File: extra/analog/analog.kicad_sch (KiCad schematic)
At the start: 0 parts

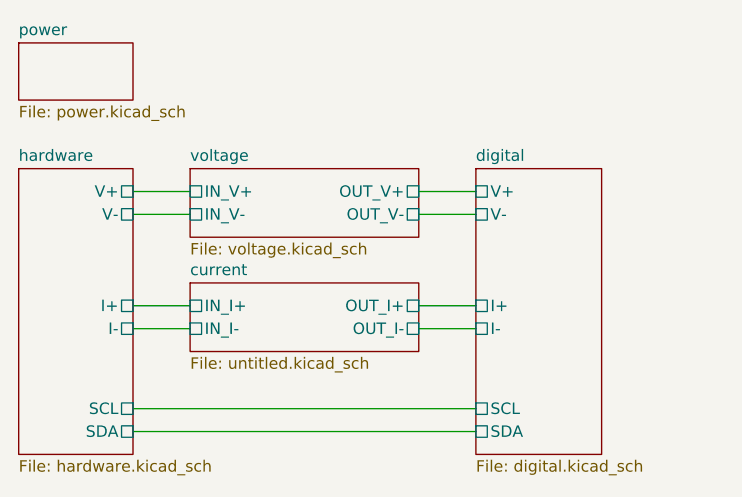
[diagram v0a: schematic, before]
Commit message: Added component values
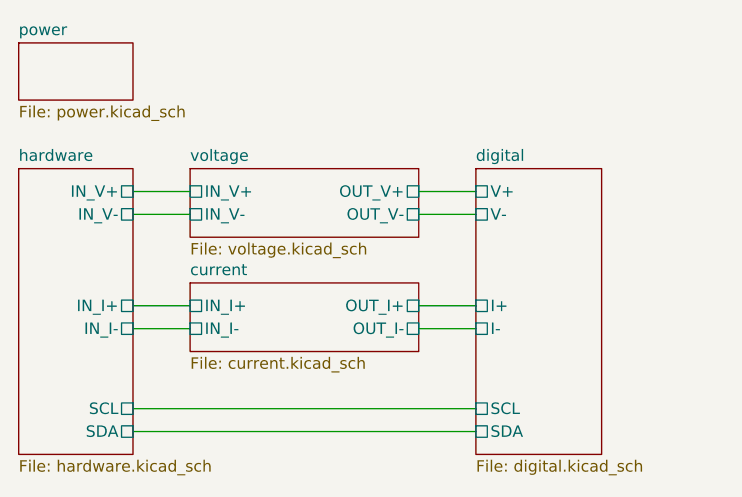
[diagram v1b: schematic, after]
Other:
- sheet current: file untitled.kicad_sch -> current.kicad_sch
- sheet hardware ports: added IN_I+, IN_I-, IN_V+, IN_V-; removed I+, I-, V+, V-
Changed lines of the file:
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@@
-			)
-		)
-		(pin "I+" passive
-			(at 77.47 78.74 0)
-			(effects
-				(font
-					(size 1.27 1.27)
-				)
-				(justify right)
-			)
-		)
-		(pin "I-" passive
-			(at 77.47 81.28 0)
-			(effects
-				(font
-					(size 1.27 1.27)
-				)
-				(justify right)
 			)
 		)
@@
 			)
 		)
-		(pin "V+" passive
+		(pin "IN_I+" passive
+			(at 77.47 78.74 0)
+			(effects
+				(font
+					(size 1.27 1.27)
+				)
+				(justify right)
+			)
+		)
+		(pin "IN_I-" passive
+			(at 77.47 81.28 0)
+			(effects
+				(font
+					(size 1.27 1.27)
+				)
+				(justify right)
+			)
+		)
+		(pin "IN_V+" passive
 			(at 77.47 66.04 0)
 			(effects
@@
 			)
 		)
-		(pin "V-" passive
+		(pin "IN_V-" passive
 			(at 77.47 68.58 0)
 			(effects
@@
 			)
 		)
-		(property "Sheetfile" "untitled.kicad_sch"
+		(property "Sheetfile" "current.kicad_sch"
 			(at 83.82 84.4046 0)
 			(effects

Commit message: Finalization with jack
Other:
- company: (none) -> jlab
- title: (none) -> Analog Frontend
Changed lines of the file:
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@@
 	(generator_version "9.0")
 	(paper "A4")
+	(title_block
+		(title "Analog Frontend")
+		(date "2026-03-13")
+		(rev "v3.0.0")
+		(company "jlab")
+	)
 	(wire
 		(pts
